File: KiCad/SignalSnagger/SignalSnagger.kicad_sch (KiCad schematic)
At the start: 62 parts, among them J102 Left, J104 Right, J105 36-5005-ND, J106 36-5006-ND, J107 36-5006-ND, J108 36-5005-ND, Q101 MMBT2222A, Q102 MMBT2222A, Q103 MMBT2222A, T101 Transformer_1P_SS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

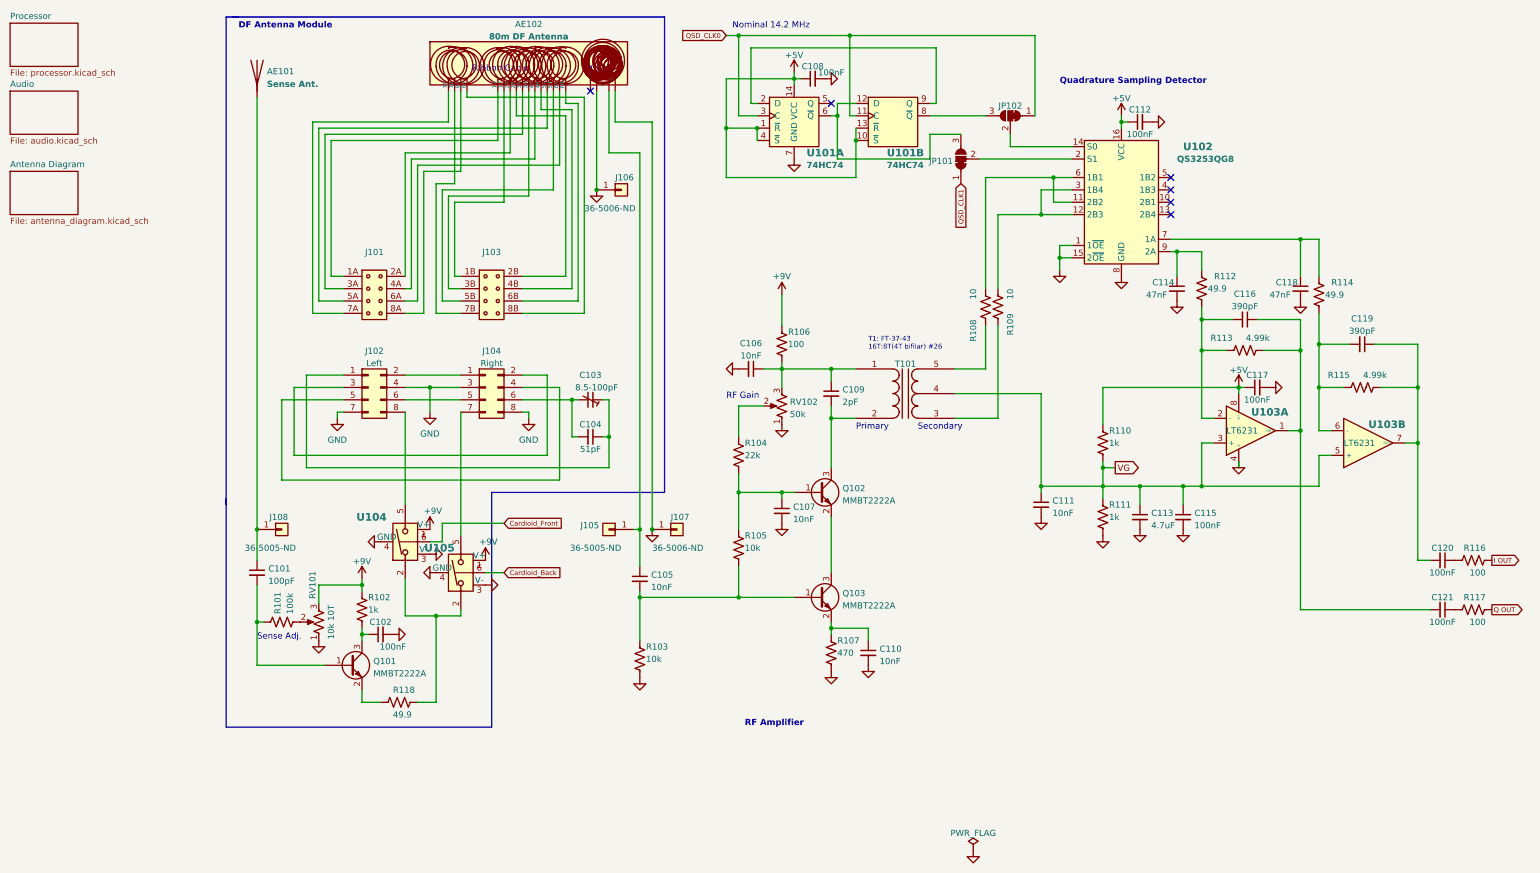
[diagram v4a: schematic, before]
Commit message: Schematic Updates
Added display and rotary encoder
Added Jerry's changes based on testing
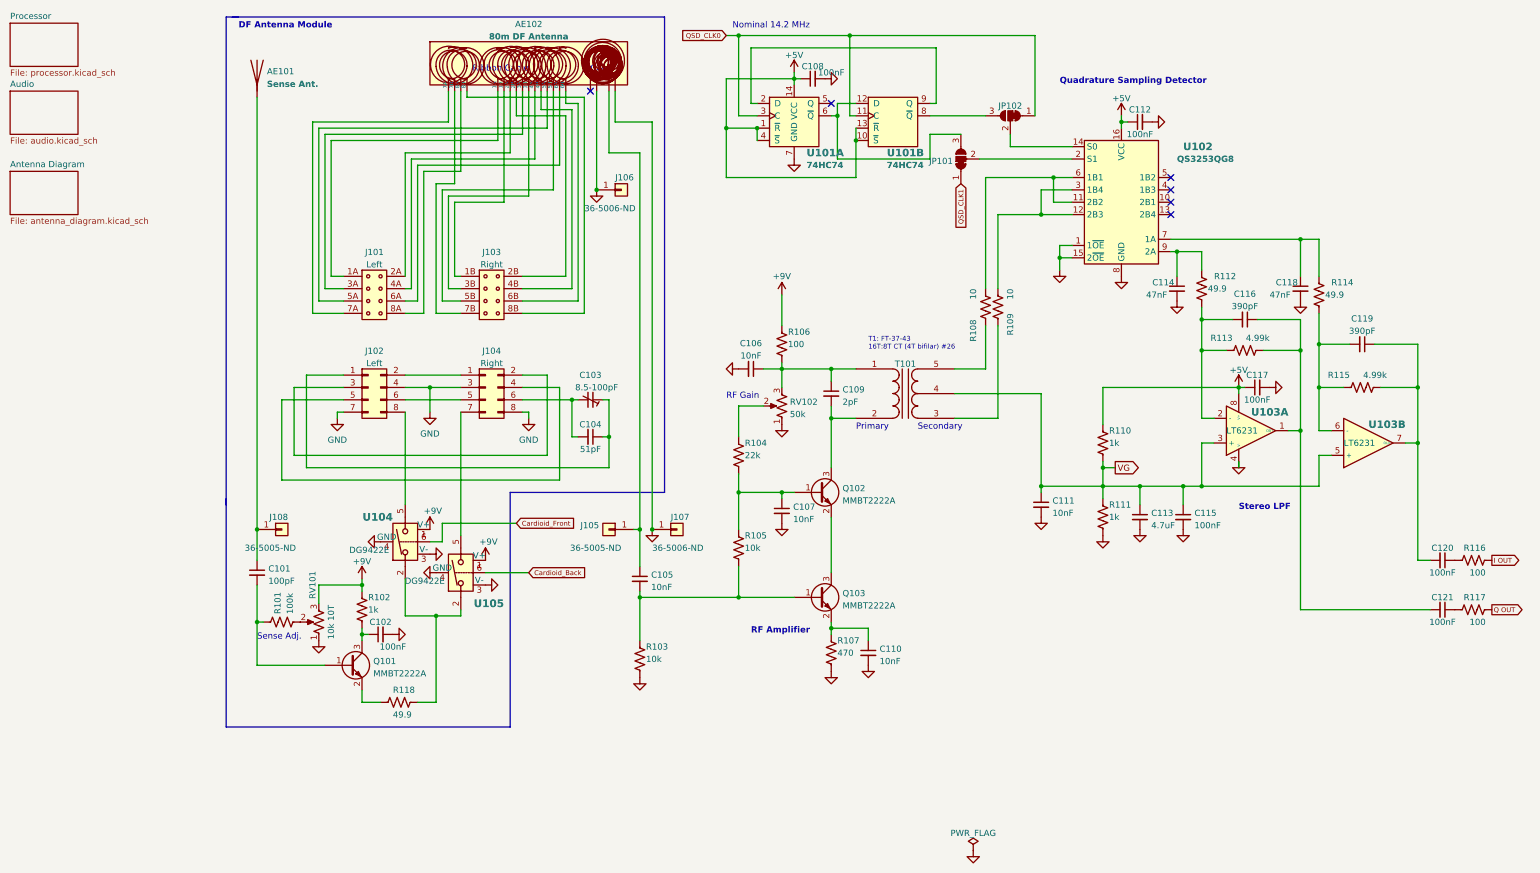
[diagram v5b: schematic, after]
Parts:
- J101: value (none) -> Left; symbol Connector_Generic:Plug_02x04_Odd_Even -> Connector:Plug_Male_Pins_02x04_Odd_Even_1
- J103: value (none) -> Right; symbol Connector_Generic:Plug_02x04_Odd_Even -> Connector:Plug_Male_Pins_02x04_Odd_Even_2
- JP102: value (none) -> SolderJumper_3_Bridged12
- U104, U105: value (none) -> DG9422E
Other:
- note added: "Stereo LPF"
- note added: "T1: FT-37-43 16T:8T CT (4T bifilar) #26"
- note removed: "T1: FT-37-43 16T:8T(4T bifilar) #26"

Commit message: Schematic Updates
Rev 0.18
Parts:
- added JP?: Jumper_2_Bridged, Jumper:Jumper_THT_1x02_P1.27mm_Vertical, symbol Jumper:Jumper_2_Bridged_THT
- added JP? (x3): (no value), Jumper:Jumper_THT_1x02_P1.27mm_Vertical, symbol Jumper:Jumper_2_Bridged_THT
- added JP?: (no value), symbol Jumper:Jumper_2_Bridged_THT
- added U106: (no value), symbol Potentiometer_Digital:AD5280
- C109: value 2pF -> (none)
- RV102: value 50k -> (none)
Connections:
- net +9V: now also U106.4 (VDD)
- net GND: now also JP?.1 (A), JP?.1 (A), U106.10 (GND), U106.11 (VSS), U106.3 (B), U106.8 (AD0), U106.9 (AD1); no longer J102.7 (Pin_7), J104.8 (Pin_8)
- net at C106.1, C109.1, R106.2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: now also U106.1 (A)
- net at R104.1, RV102.2: now also U106.2 (W)
- net at J104.7 (Pin_7): now also JP?.2 (B); no longer U105.5
- net at U104.2, U105.2: now also JP?.2 (B); no longer R118.1
- net at U104.5: now also JP?.1 (A); no longer J102.8 (Pin_8)
- new net: J104.8 (Pin_8), JP?.2 (B)
- new net: JP?.1 (A), R118.1
- new net: J102.7 (Pin_7), JP?.2 (B)
- new net: J102.8 (Pin_8), JP?.2 (B)
- new net: JP?.1 (A), U105.5
- new net +3V3: U106.13 (VLOG), U106.5 (~{SHDN})
- new net SCL1: U106.6 (SCL)
- new net SDA1: U106.7 (SDA)
- no-connect marks 6 -> 8
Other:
- moved on the sheet: C105, C107, C109, C110, C111, Q102, Q103, R103, R104, R105, R107, R108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

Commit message: Annotated Schematic
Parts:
- gave numbers to parts that had none: 5
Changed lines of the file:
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@@
   (symbol (lib_name "Jumper_2_Bridged_THT_3") (lib_id "Jumper:Jumper_2_Bridged_THT") (at 58.42 147.32 90) (unit 1)
     (in_bom yes) (on_board yes)
-    (property "Reference" "JP?" (id 0) (at 59.69 147.32 90)
+    (property "Reference" "JP105" (id 0) (at 59.69 147.32 90)
       (effects (font (size 1.27 1.27)) (justify right))
     )
@@
   (symbol (lib_name "Jumper_2_Bridged_THT_1") (lib_id "Jumper:Jumper_2_Bridged_THT") (at 39.37 102.87 90) (unit 1)
     (in_bom yes) (on_board yes)
-    (property "Reference" "JP?" (id 0) (at 40.64 102.87 90)
+    (property "Reference" "JP103" (id 0) (at 40.64 105.41 90)
       (effects (font (size 1.27 1.27)) (justify right))
     )
@@
   (symbol (lib_id "Jumper:Jumper_2_Bridged_THT") (at 77.47 102.87 90) (unit 1)
     (in_bom yes) (on_board yes)
-    (property "Reference" "JP?" (id 0) (at 72.39 102.87 90)
+    (property "Reference" "JP107" (id 0) (at 69.85 101.6 90)
       (effects (font (size 1.27 1.27)) (justify right))
     )
@@
   (symbol (lib_name "Jumper_2_Bridged_THT_3") (lib_id "Jumper:Jumper_2_Bridged_THT") (at 63.5 102.87 90) (unit 1)
     (in_bom yes) (on_board yes)
-    (property "Reference" "JP?" (id 0) (at 64.77 102.87 90)
+    (property "Reference" "JP106" (id 0) (at 64.77 105.41 90)
       (effects (font (size 1.27 1.27)) (justify right))
     )
@@
   (symbol (lib_name "Jumper_2_Bridged_THT_2") (lib_id "Jumper:Jumper_2_Bridged_THT") (at 52.07 102.87 90) (unit 1)
     (in_bom yes) (on_board yes)
-    (property "Reference" "JP?" (id 0) (at 45.72 102.87 90)
+    (property "Reference" "JP104" (id 0) (at 44.45 101.6 90)
       (effects (font (size 1.27 1.27)) (justify right))
     )
@@
       (reference "JP102") (unit 1) (value "SolderJumper_3_Bridged12") (footprint "")
     )
+    (path "/a02b79db-cd64-4fe6-a4ff-546efbbc5258"
+      (reference "JP103") (unit 1) (value "Jumper_2_Bridged") (footprint "Jumper:Jumper_THT_1x02_P1.27mm_Vertical")
+    )
+    (path "/ddb06994-986b-4c62-b6b5-f2ee0d80bb9e"
+      (reference "JP104") (unit 1) (value "Jumper_2_Bridged") (footprint "Jumper:Jumper_THT_1x02_P1.27mm_Vertical")
+    )
     (path "/5170ca02-dda1-4bb5-8bb3-5970dd0c5024"
-      (reference "JP?") (unit 1) (value "Jumper_2_Bridged") (footprint "Jumper:Jumper_THT_1x02_P1.27mm_Vertical")
-    )
-    (path "/a02b79db-cd64-4fe6-a4ff-546efbbc5258"
-      (reference "JP?") (unit 1) (value "Jumper_2_Bridged") (footprint "Jumper:Jumper_THT_1x02_P1.27mm_Vertical")
+      (reference "JP105") (unit 1) (value "Jumper_2_Bridged") (footprint "Jumper:Jumper_THT_1x02_P1.27mm_Vertical")
+    )
+    (path "/b74ca561-f165-41a3-ba71-bf404ed79ef8"
+      (reference "JP106") (unit 1) (value "Jumper_2_Bridged") (footprint "Jumper:Jumper_THT_1x02_P1.27mm_Vertical")
     )
     (path "/a7598143-c189-4cf9-919e-4196ff6b9ca2"
-      (reference "JP?") (unit 1) (value "Jumper_2_Bridged") (footprint "Jumper:Jumper_THT_1x02_P1.27mm_Vertical")
-    )
-    (path "/b74ca561-f165-41a3-ba71-bf404ed79ef8"
-      (reference "JP?") (unit 1) (value "Jumper_2_Bridged") (footprint "Jumper:Jumper_THT_1x02_P1.27mm_Vertical")
-    )
-    (path "/ddb06994-986b-4c62-b6b5-f2ee0d80bb9e"
-      (reference "JP?") (unit 1) (value "Jumper_2_Bridged") (footprint "Jumper:Jumper_THT_1x02_P1.27mm_Vertical")
+      (reference "JP107") (unit 1) (value "Jumper_2_Bridged") (footprint "Jumper:Jumper_THT_1x02_P1.27mm_Vertical")
     )
     (path "/b7e6c0d8-791a-469a-85d5-f8e886443224/21bc3a5f-79ed-4932-8b06-ea4e48e4f139"

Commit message: Schematic Tweaks
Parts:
- JP105: value Jumper_2_Bridged -> (none)
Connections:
- net +9V renamed +VSW
